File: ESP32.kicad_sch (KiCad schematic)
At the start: 8 parts, among them J1 Micro_SD_Card, SW1 RESET, SW2 BOOT, U3 ESP32-S3-WROOM-1

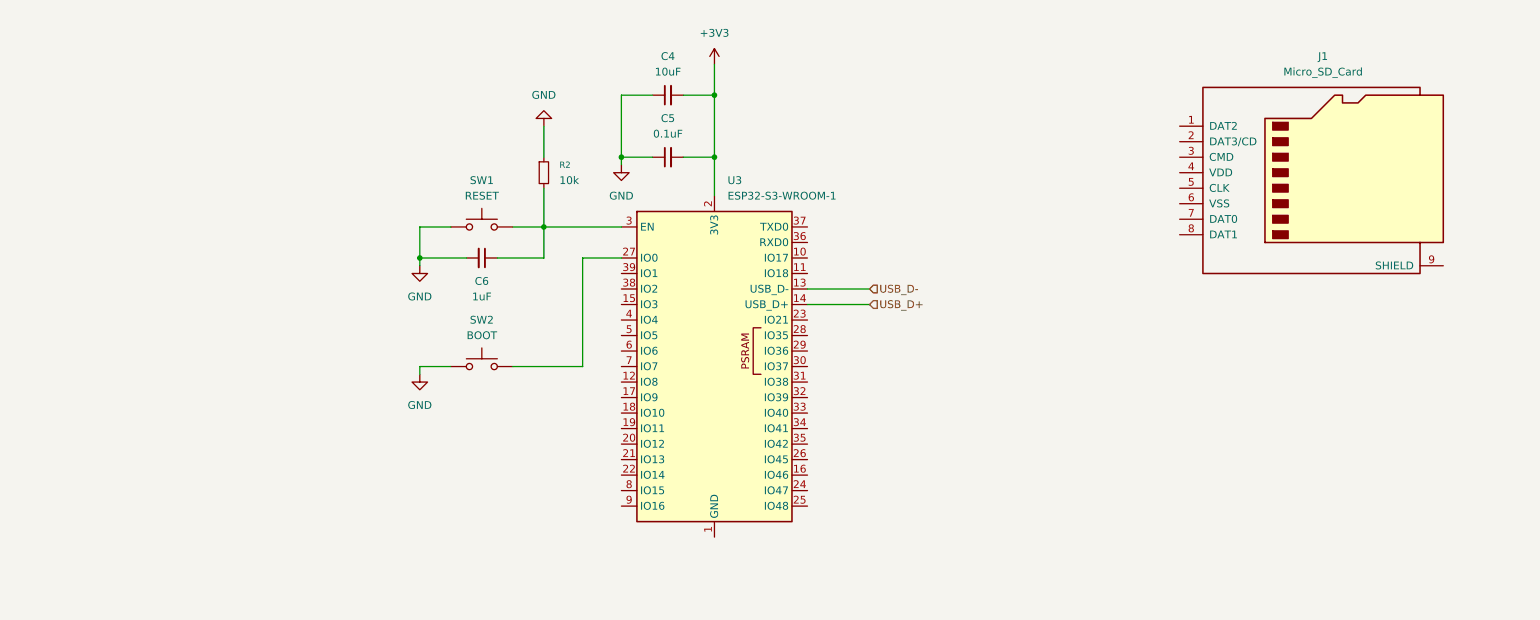
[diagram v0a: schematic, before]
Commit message: add esp logic for speaker and lcd
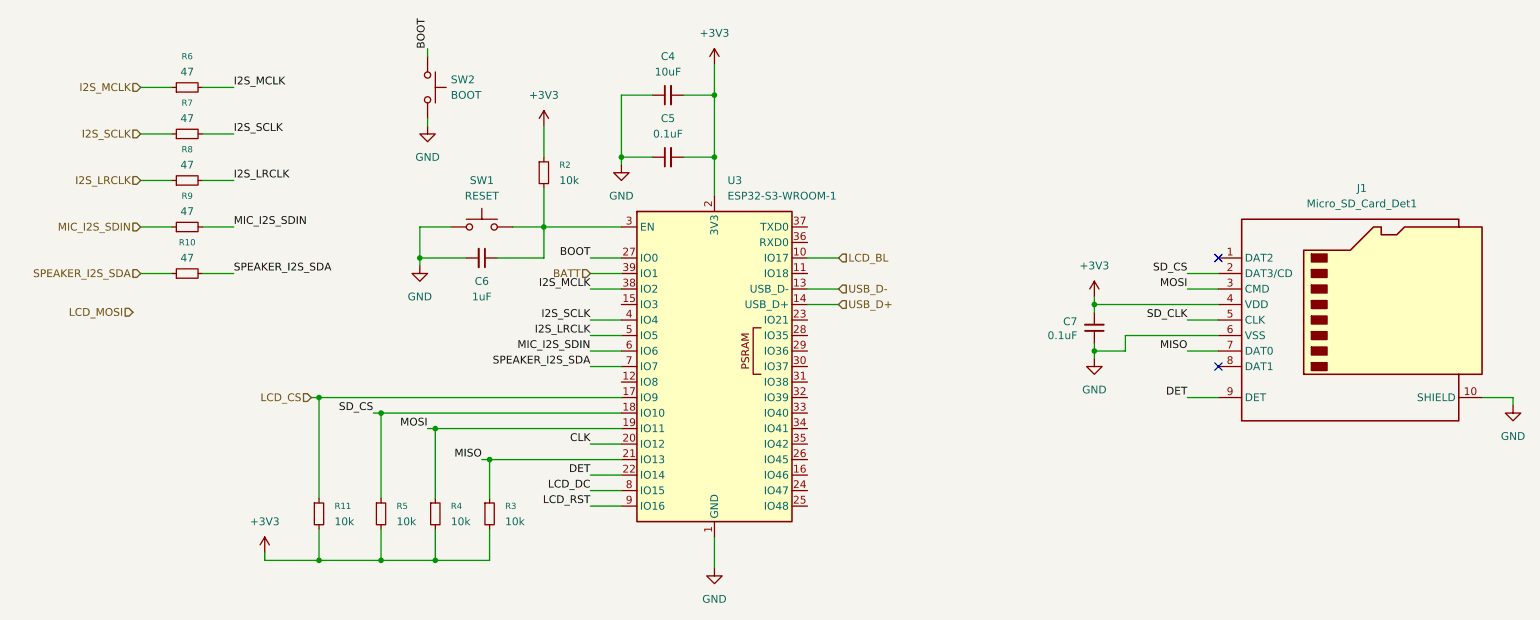
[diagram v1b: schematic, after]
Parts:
- removed J1: Micro_SD_Card, symbol Connector:Micro_SD_Card
- added C7: 0.1uF, symbol Device:C_Small
- added J1: Micro_SD_Card_Det1, symbol Connector:Micro_SD_Card_Det1
- added R10, R6, R7, R8, R9: 47, symbol Device:R_Small
- added R11, R3, R4, R5: 10k, symbol Device:R_Small
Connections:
- net +3V3: now also R2.1, C7.2, J1.4 (VDD), R11.2, R3.2, R4.2, R5.2
- net GND: now also SW2.2, U3.1 (GND), U3.40 (GND), U3.41 (GND), C7.1, J1.10 (SHIELD), J1.6 (VSS); no longer R2.1, SW2.1
- net BOOT: now reaches U3.27 (IO0)
- net BOOT: now also SW2.1; no longer SW2.2
- net LCD_BL: now reaches U3.10 (IO17)
- net LCD_CS: now reaches U3.17 (IO9)
- net LCD_CS: now also R11.1
- net SD_CS: now reaches U3.18 (IO10)
- net SD_CS: now also J1.2 (DAT3/CD), R5.1
- net MOSI: now reaches U3.19 (IO11)
- net MOSI: now also J1.3 (CMD), R4.1
- net CLK: now reaches U3.20 (IO12)
- net MISO: now reaches U3.21 (IO13)
- net MISO: now also J1.7 (DAT0), R3.1
- net DET: now reaches U3.22 (IO14)
- net DET: now also J1.9 (DET)
- net I2S_MCLK: now reaches U3.38 (IO2)
- net I2S_MCLK: now also R6.1, R6.2
- net BATT: now reaches U3.39 (IO1)
- net I2S_SCLK: now reaches U3.4 (IO4)
- net I2S_SCLK: now also R7.1, R7.2
- net I2S_LRCLK: now reaches U3.5 (IO5)
- net I2S_LRCLK: now also R8.1, R8.2
- net MIC_I2S_SDIN: now reaches U3.6 (IO6)
- net MIC_I2S_SDIN: now also R9.1, R9.2
- net SPEAKER_I2S_SDA: now reaches U3.7 (IO7)
- net SPEAKER_I2S_SDA: now also R10.1, R10.2
- net LCD_DC: now reaches U3.8 (IO15)
- net LCD_RST: now reaches U3.9 (IO16)
- new net SD_CLK: J1.5 (CLK)
- no-connect marks 0 -> 2
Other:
- moved on the sheet: SW2

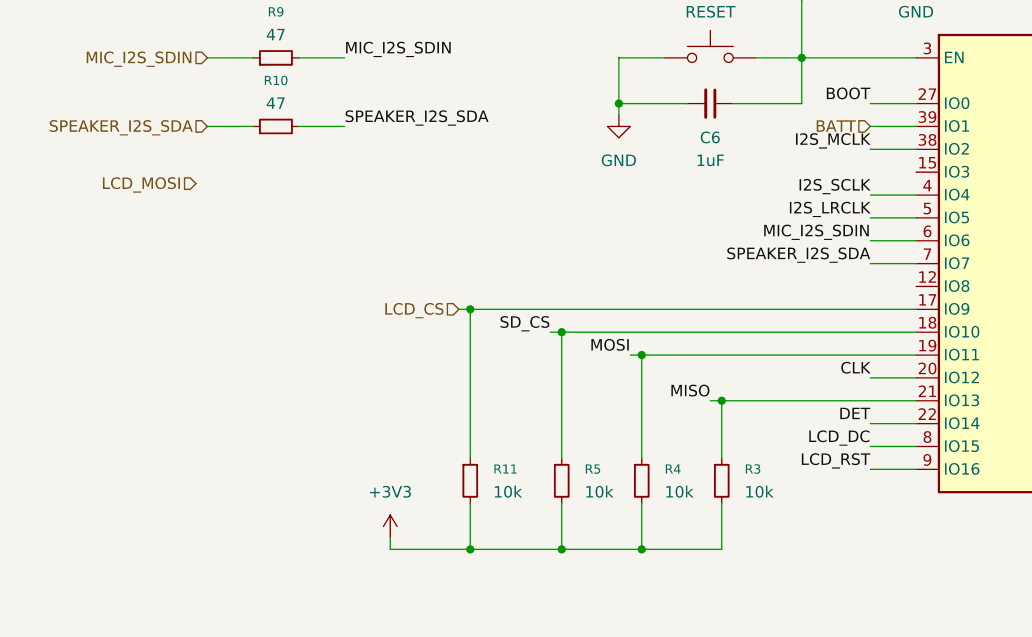
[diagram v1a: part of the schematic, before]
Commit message: finish esp32 hierarchical flags
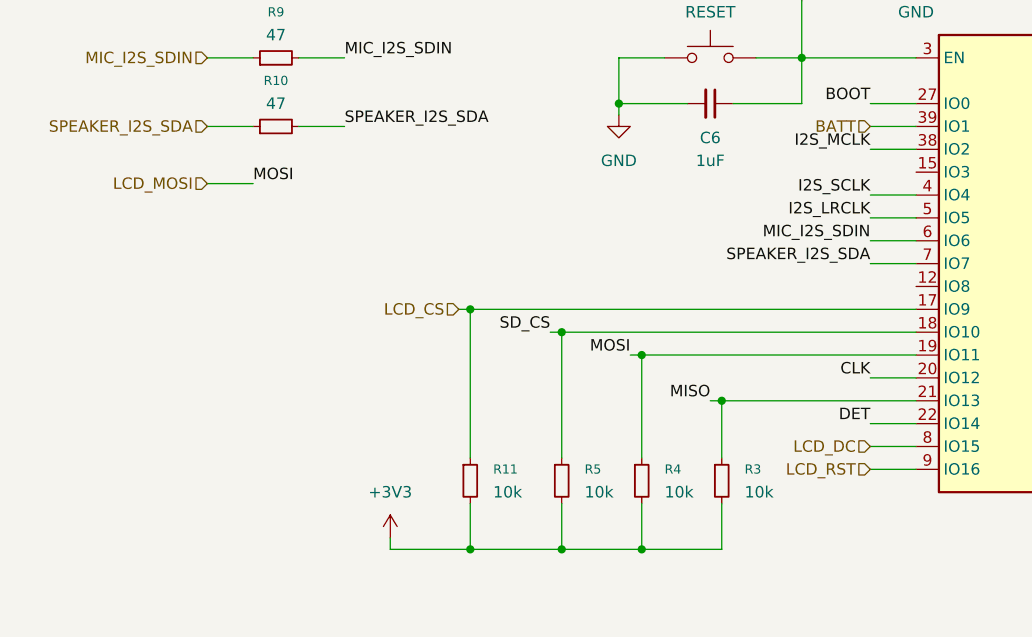
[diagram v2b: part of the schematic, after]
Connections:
- net MOSI is gone; now on net LCD_MOSI: J1.3 (CMD), R4.1, U3.19 (IO11)
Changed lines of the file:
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@@
+	(wire
+		(pts
+			(xy 48.26 83.82) (xy 53.34 83.82)
+		)
+		(stroke
+			(width 0)
+			(type default)
+		)
+	)
 	(wire
 		(pts
@@
 		)
 	)
+	(label "MOSI"
+		(at 53.34 83.82 0)
+		(effects
+			(font
+				(size 1.27 1.27)
+			)
+			(justify left bottom)
+		)
+	)
 	(label "SPEAKER_I2S_SDA"
 		(at 63.5 77.47 0)
@@
 		)
 	)
-	(label "LCD_DC"
-		(at 121.92 113.03 180)
-		(effects
-			(font
-				(size 1.27 1.27)
-			)
-			(justify right bottom)
-		)
-	)
 	(label "MISO"
 		(at 219.71 90.17 180)
@@
 		)
 	)
-	(label "LCD_RST"
-		(at 121.92 115.57 180)
-		(effects
-			(font
-				(size 1.27 1.27)
-			)
-			(justify right bottom)
-		)
-	)
 	(label "SD_CLK"
 		(at 219.71 85.09 180)
@@
 	(hierarchical_label "LCD_MOSI"
 		(shape input)
-		(at 46.99 83.82 180)
+		(at 48.26 83.82 180)
 		(effects
 			(font
@@
 		)
 	)
+	(hierarchical_label "LCD_DC"
+		(shape input)
+		(at 121.92 113.03 180)
+		(effects
+			(font
+				(size 1.27 1.27)
+			)
+			(justify right)
+		)
+	)
 	(hierarchical_label "I2S_LRCLK"
 		(shape input)
@@
 		(effects
 			(font
+				(size 1.27 1.27)
+			)
+			(justify right)
+		)
+	)
+	(hierarchical_label "LCD_RST"
+		(shape input)
+		(at 121.92 115.57 180)
+		(effects
+			(font

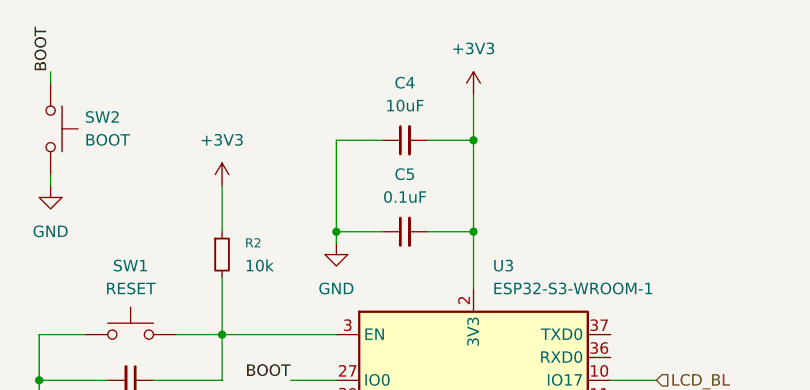
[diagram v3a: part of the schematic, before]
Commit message: fix esp decoupling capacitor value
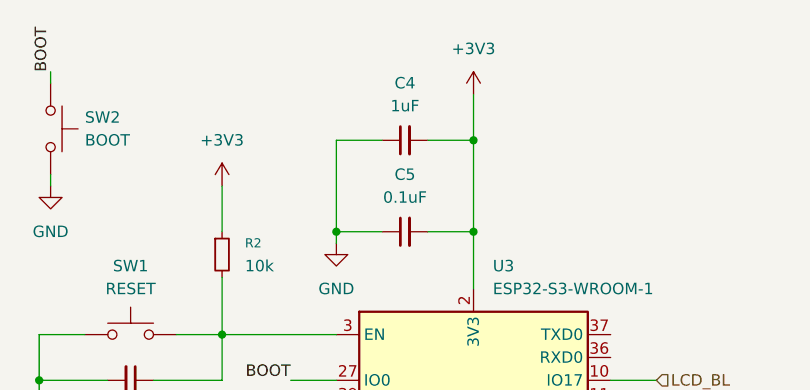
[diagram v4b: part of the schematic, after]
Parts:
- C4: value 10uF -> 1uF
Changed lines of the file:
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@@
 		)
 		(instances
-			(project ""
+			(project "carrot-voice-recorder"
 				(path "/6e73c62c-3b38-4fda-9d84-b2b702c58c74/f3f83793-a55c-4bdb-88d3-df48ab154e45"
 					(reference "#PWR010")
@@
 		)
 		(instances
-			(project ""
+			(project "carrot-voice-recorder"
 				(path "/6e73c62c-3b38-4fda-9d84-b2b702c58c74/f3f83793-a55c-4bdb-88d3-df48ab154e45"
 					(reference "#PWR016")
@@
 		)
 		(instances
-			(project ""
+			(project "carrot-voice-recorder"
 				(path "/6e73c62c-3b38-4fda-9d84-b2b702c58c74/f3f83793-a55c-4bdb-88d3-df48ab154e45"
 					(reference "R3")
@@
 		)
 		(instances
-			(project ""
+			(project "carrot-voice-recorder"
 				(path "/6e73c62c-3b38-4fda-9d84-b2b702c58c74/f3f83793-a55c-4bdb-88d3-df48ab154e45"
 					(reference "C5")
@@
 		)
 		(instances
-			(project ""
+			(project "carrot-voice-recorder"
 				(path "/6e73c62c-3b38-4fda-9d84-b2b702c58c74/f3f83793-a55c-4bdb-88d3-df48ab154e45"
 					(reference "SW2")
@@
 		)
 		(instances
-			(project ""
+			(project "carrot-voice-recorder"
 				(path "/6e73c62c-3b38-4fda-9d84-b2b702c58c74/f3f83793-a55c-4bdb-88d3-df48ab154e45"
 					(reference "#PWR012")
@@
 		)
 		(instances
-			(project ""
+			(project "carrot-voice-recorder"
 				(path "/6e73c62c-3b38-4fda-9d84-b2b702c58c74/f3f83793-a55c-4bdb-88d3-df48ab154e45"
 					(reference "#PWR014")
@@
 		)
 		(instances
-			(project ""
+			(project "carrot-voice-recorder"
 				(path "/6e73c62c-3b38-4fda-9d84-b2b702c58c74/f3f83793-a55c-4bdb-88d3-df48ab154e45"
 					(reference "U3")
@@
 		)
 		(instances
-			(project ""
+			(project "carrot-voice-recorder"
 				(path "/6e73c62c-3b38-4fda-9d84-b2b702c58c74/f3f83793-a55c-4bdb-88d3-df48ab154e45"
 					(reference "C7")
@@
 		)
 		(instances
-			(project ""
+			(project "carrot-voice-recorder"
 				(path "/6e73c62c-3b38-4fda-9d84-b2b702c58c74/f3f83793-a55c-4bdb-88d3-df48ab154e45"
 					(reference "R9")
@@
 		)
 		(instances
-			(project ""
+			(project "carrot-voice-recorder"
 				(path "/6e73c62c-3b38-4fda-9d84-b2b702c58c74/f3f83793-a55c-4bdb-88d3-df48ab154e45"
 					(reference "#PWR08")
@@
 		)
 		(instances
-			(project ""
+			(project "carrot-voice-recorder"
 				(path "/6e73c62c-3b38-4fda-9d84-b2b702c58c74/f3f83793-a55c-4bdb-88d3-df48ab154e45"
 					(reference "#PWR017")
@@
 		)
 		(instances
-			(project ""
+			(project "carrot-voice-recorder"
 				(path "/6e73c62c-3b38-4fda-9d84-b2b702c58c74/f3f83793-a55c-4bdb-88d3-df48ab154e45"
 					(reference "C6")
@@
 		)
 		(instances
-			(project ""
+			(project "carrot-voice-recorder"
 				(path "/6e73c62c-3b38-4fda-9d84-b2b702c58c74/f3f83793-a55c-4bdb-88d3-df48ab154e45"
 					(reference "R10")
@@
 		)
 		(instances
-			(project ""
+			(project "carrot-voice-recorder"
 				(path "/6e73c62c-3b38-4fda-9d84-b2b702c58c74/f3f83793-a55c-4bdb-88d3-df48ab154e45"
 					(reference "R8")
@@
 		)
 		(instances
-			(project ""
+			(project "carrot-voice-recorder"
 				(path "/6e73c62c-3b38-4fda-9d84-b2b702c58c74/f3f83793-a55c-4bdb-88d3-df48ab154e45"
 					(reference "R4")
@@
 		)
 		(instances
-			(project ""
+			(project "carrot-voice-recorder"
 				(path "/6e73c62c-3b38-4fda-9d84-b2b702c58c74/f3f83793-a55c-4bdb-88d3-df48ab154e45"
 					(reference "#PWR015")
@@
 		)
 		(instances
-			(project ""
+			(project "carrot-voice-recorder"
 				(path "/6e73c62c-3b38-4fda-9d84-b2b702c58c74/f3f83793-a55c-4bdb-88d3-df48ab154e45"
 					(reference "R5")
@@
 			)
 		)
-		(property "Value" "10uF"
+		(property "Value" "1uF"
 			(at 134.6263 44.45 90)
 			(effects
@@
 		)
 		(instances
-			(project ""
+			(project "carrot-voice-recorder"
 				(path "/6e73c62c-3b38-4fda-9d84-b2b702c58c74/f3f83793-a55c-4bdb-88d3-df48ab154e45"
 					(reference "C4")
@@
 		)
 		(instances
-			(project ""
+			(project "carrot-voice-recorder"
 				(path "/6e73c62c-3b38-4fda-9d84-b2b702c58c74/f3f83793-a55c-4bdb-88d3-df48ab154e45"
 					(reference "R2")
@@
 		)
 		(instances
-			(project ""
+			(project "carrot-voice-recorder"
 				(path "/6e73c62c-3b38-4fda-9d84-b2b702c58c74/f3f83793-a55c-4bdb-88d3-df48ab154e45"
 					(reference "J1")
@@
 		)
 		(instances
-			(project ""
+			(project "carrot-voice-recorder"
 				(path "/6e73c62c-3b38-4fda-9d84-b2b702c58c74/f3f83793-a55c-4bdb-88d3-df48ab154e45"
 					(reference "#PWR09")
@@
 		)
 		(instances
-			(project ""
+			(project "carrot-voice-recorder"
 				(path "/6e73c62c-3b38-4fda-9d84-b2b702c58c74/f3f83793-a55c-4bdb-88d3-df48ab154e45"
 					(reference "R6")
@@
 		)
 		(instances
-			(project ""
+			(project "carrot-voice-recorder"
 				(path "/6e73c62c-3b38-4fda-9d84-b2b702c58c74/f3f83793-a55c-4bdb-88d3-df48ab154e45"
 					(reference "SW1")
@@
 		)
 		(instances
-			(project ""
+			(project "carrot-voice-recorder"
 				(path "/6e73c62c-3b38-4fda-9d84-b2b702c58c74/f3f83793-a55c-4bdb-88d3-df48ab154e45"
 					(reference "R7")
@@
 		)
 		(instances
-			(project ""
+			(project "carrot-voice-recorder"
 				(path "/6e73c62c-3b38-4fda-9d84-b2b702c58c74/f3f83793-a55c-4bdb-88d3-df48ab154e45"
 					(reference "#PWR013")
